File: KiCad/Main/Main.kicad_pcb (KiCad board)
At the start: 2 copper layers, 78 x 69.5 mm, 0 parts

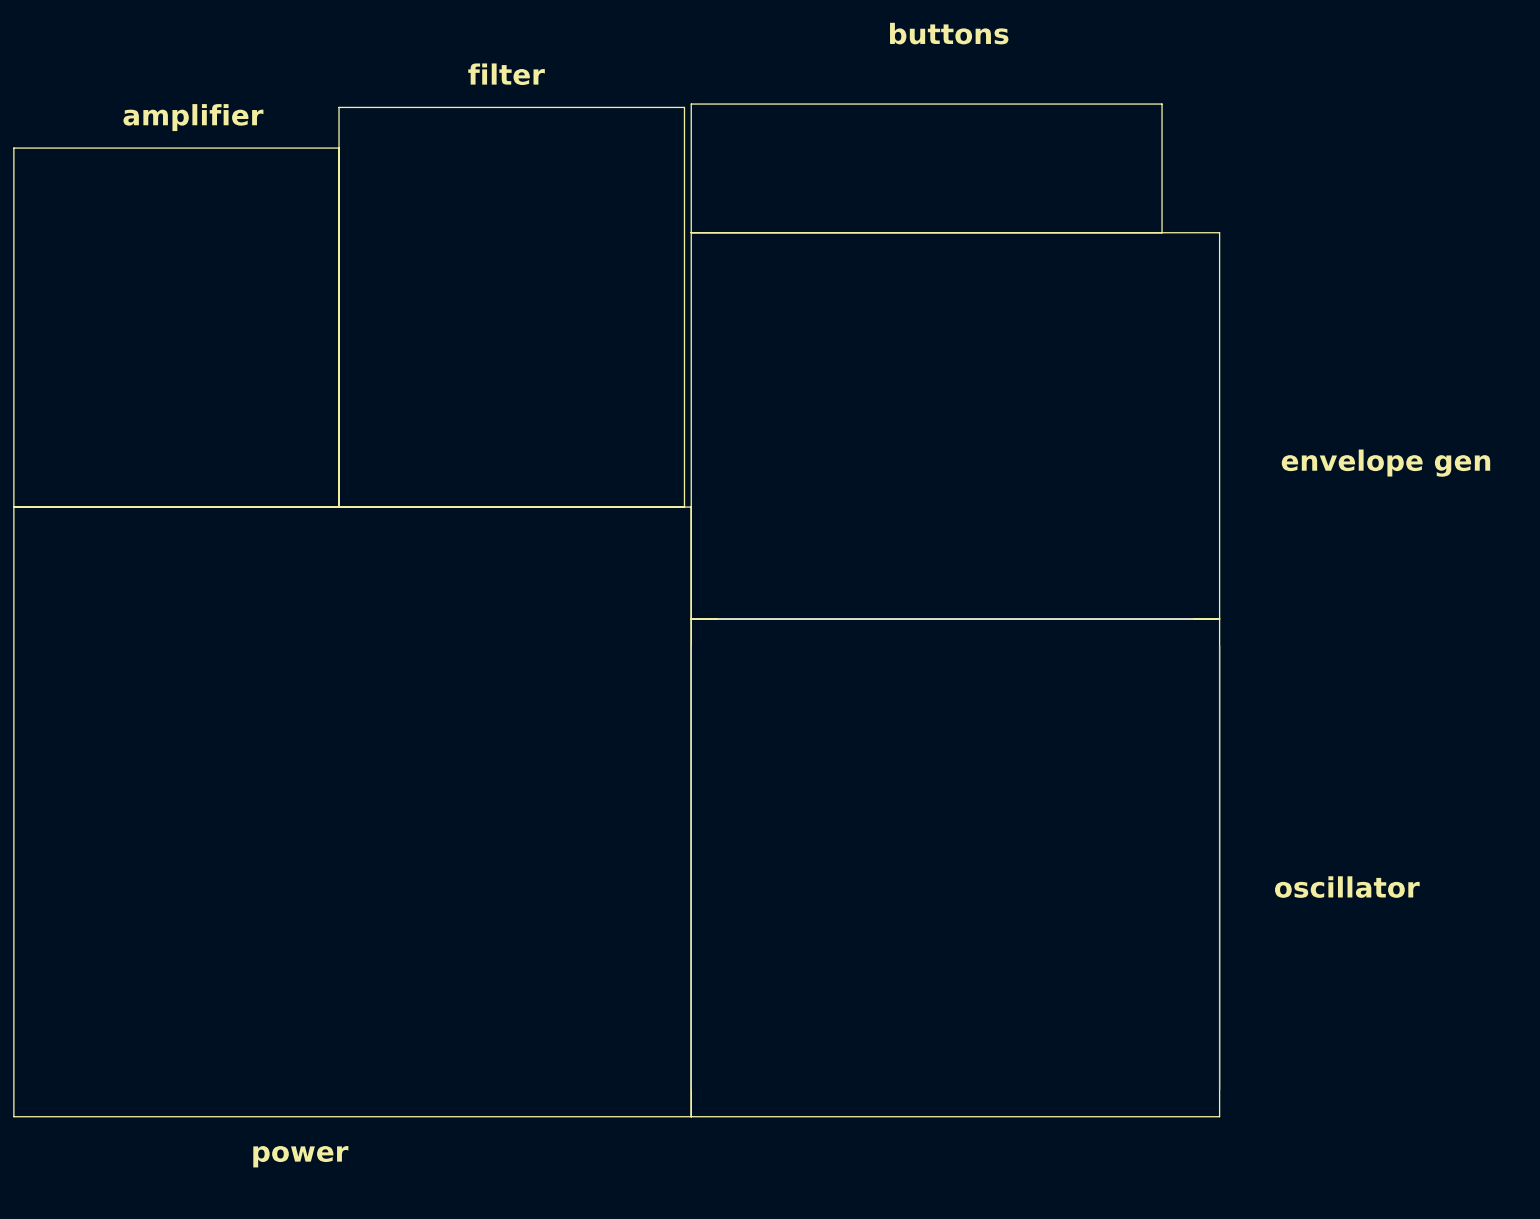
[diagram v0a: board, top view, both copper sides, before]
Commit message: merged project into one combined board (excluding the buttons)
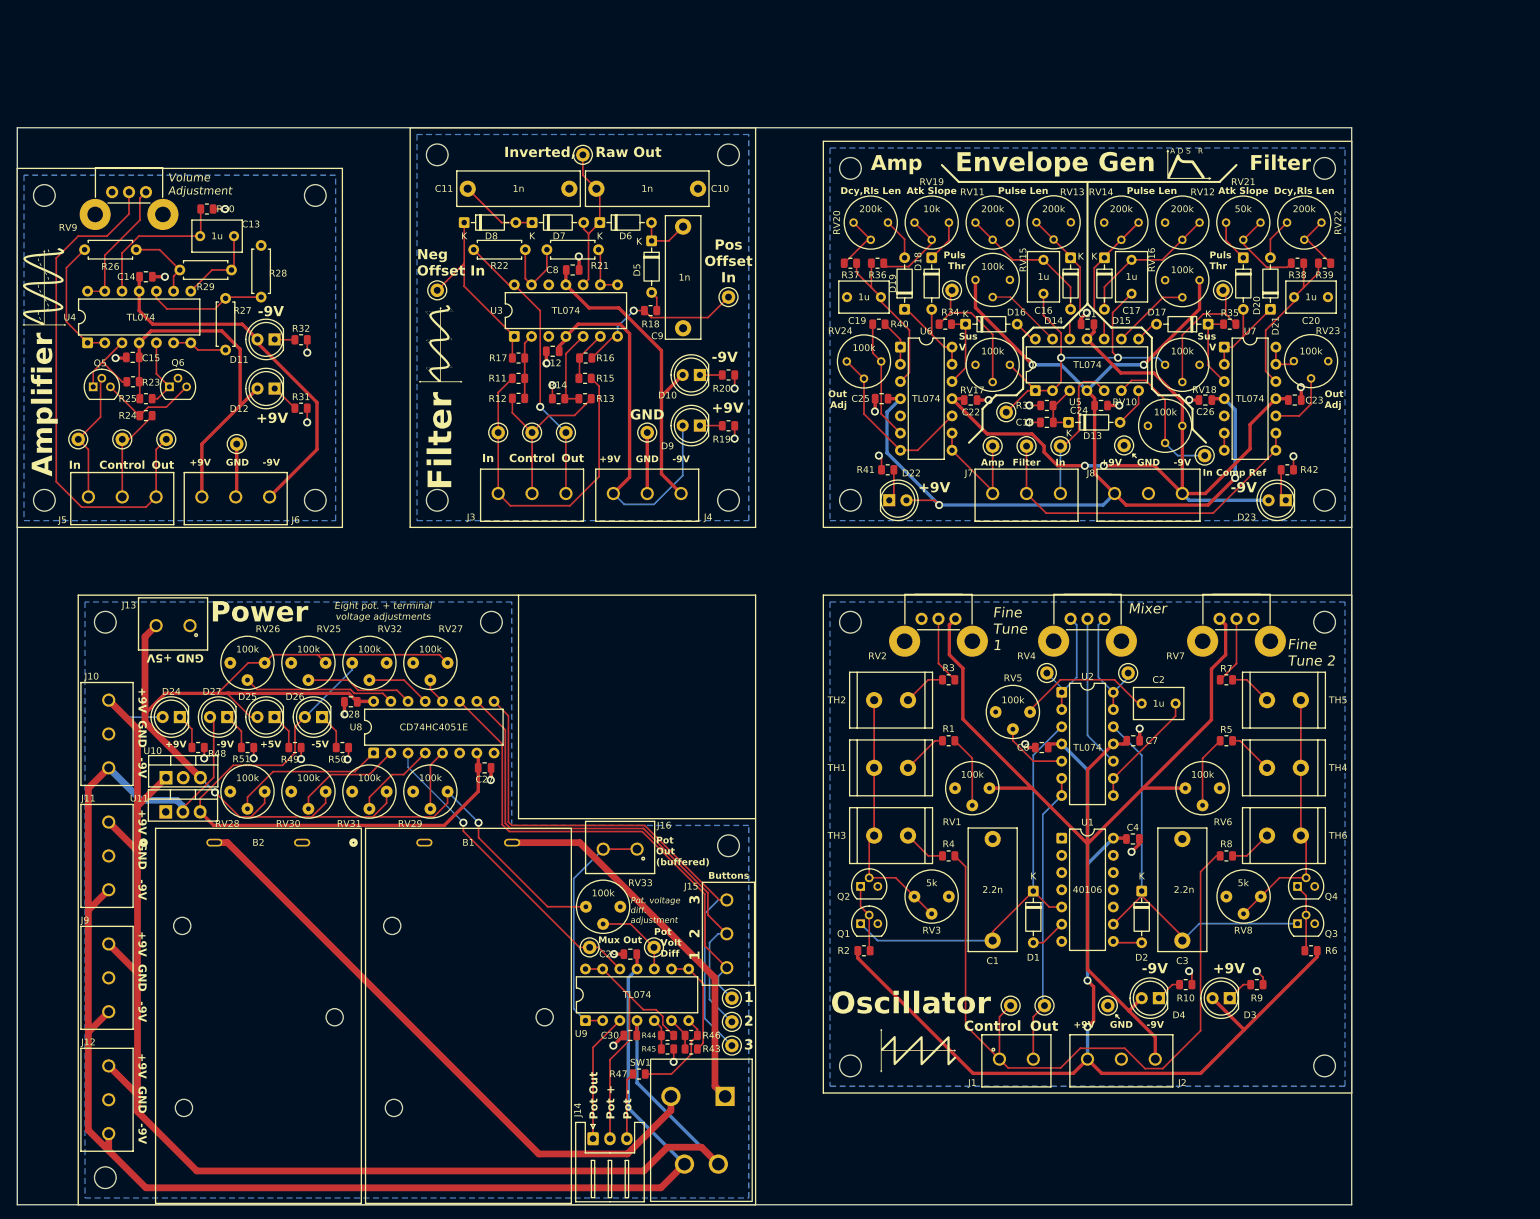
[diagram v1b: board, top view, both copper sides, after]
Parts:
- added B1: BC9VPC, Battery Holder BC9VPC:BC9VPC_MPD, F.Cu at (78.6, 124.5)
- added B2: BC9VPC, Battery Holder BC9VPC:BC9VPC_MPD, F.Cu at (47.6, 124.5)
- added C1: 2.2n, Capacitor_THT:C_Rect_L18.0mm_W7.0mm_P15.00mm_FKS3_FKP3, F.Cu at (162.5, 139.0)
- added C10: 1n, Capacitor_THT:C_Rect_L18.0mm_W5.0mm_P15.00mm_FKS3_FKP3, F.Cu at (119.0, 28.0)
- added C11: 1n, Capacitor_THT:C_Rect_L18.0mm_W5.0mm_P15.00mm_FKS3_FKP3, F.Cu at (100.0, 28.0)
- added C12: 0.1u, Capacitor_SMD:C_0805_2012Metric, F.Cu at (97.5, 52.0)
- added C13: 1u, Capacitor_THT:C_Rect_L7.2mm_W4.5mm_P5.00mm, F.Cu at (50.5, 35.0)
- added C14: 0.1u, Capacitor_SMD:C_0805_2012Metric, F.Cu at (37.5, 41.0)
- added C15: 0.1u, Capacitor_SMD:C_0805_2012Metric, F.Cu at (35.5, 52.9)
- added C16: 1u, Capacitor_THT:C_Rect_L7.2mm_W4.5mm_P5.00mm, F.Cu at (170.0, 43.5)
- added C17: 1u, Capacitor_THT:C_Rect_L7.2mm_W4.5mm_P5.00mm, F.Cu at (183.0, 43.5)
- added C18: 10n, Capacitor_SMD:C_0805_2012Metric, F.Cu at (170.5, 62.5)
- added C19: 1u, Capacitor_THT:C_Rect_L7.2mm_W4.5mm_P5.00mm, F.Cu at (141.0, 44.0)
- added C2: 1u, Capacitor_THT:C_Rect_L7.2mm_W4.5mm_P5.00mm, F.Cu at (189.5, 104.0)
- added C20: 1u, Capacitor_THT:C_Rect_L7.2mm_W4.5mm_P5.00mm, F.Cu at (212.0, 44.0)
- added C21: 0.1u, Capacitor_SMD:C_0805_2012Metric, F.Cu at (176.5, 48.0)
- added C22: 0.1u, Capacitor_SMD:C_0805_2012Metric, F.Cu at (159.2, 59.2)
- added C23: 0.1u, Capacitor_SMD:C_0805_2012Metric, F.Cu at (207.1, 59.2)
- added C24: 0.1u, Capacitor_SMD:C_0805_2012Metric, F.Cu at (178.5, 60.0)
- added C25: 0.1u, Capacitor_SMD:C_0805_2012Metric, F.Cu at (146.1, 59.0)
- added C26: 0.1u, Capacitor_SMD:C_0805_2012Metric, F.Cu at (193.9, 59.2)
- added C27: 0.1u, Capacitor_SMD:C_0805_2012Metric, F.Cu at (87.5, 113.5)
- added C28: 0.1u, Capacitor_SMD:C_0805_2012Metric, F.Cu at (67.8, 103.8)
- added C29: 0.1u, Capacitor_SMD:C_0805_2012Metric, F.Cu at (109.0, 141.0)
- added C3: 2.2n, Capacitor_THT:C_Rect_L18.0mm_W7.0mm_P15.00mm_FKS3_FKP3, F.Cu at (190.5, 139.0)
- added C30: 0.1u, Capacitor_SMD:C_0805_2012Metric, F.Cu at (109.0, 153.0)
- added C4: 0.1u, Capacitor_SMD:C_0805_2012Metric, F.Cu at (183.2, 124.0)
- added C6: 0.1u, Capacitor_SMD:C_0805_2012Metric, F.Cu at (169.8, 110.5)
- added C7: 0.1u, Capacitor_SMD:C_0805_2012Metric, F.Cu at (183.2, 109.5)
- added C8: 0.1u, Capacitor_SMD:C_0805_2012Metric, F.Cu at (100.5, 40.0)
- added C9: 1n, Capacitor_THT:C_Rect_L18.0mm_W5.0mm_P15.00mm_FKS3_FKP3, F.Cu at (116.8, 48.6)
- added D1: 1N4148, Diode_THT:D_DO-35_SOD27_P7.62mm_Horizontal, F.Cu at (168.5, 131.7)
- added D10: LED, LED_THT:LED_D5.0mm, F.Cu at (119.3, 55.5)
- added D11: LED, LED_THT:LED_D5.0mm, F.Cu at (56.5, 57.5)
- added D12: LED, LED_THT:LED_D5.0mm, F.Cu at (56.5, 50.2)
- added D13: 1N4148, Diode_THT:D_DO-35_SOD27_P7.62mm_Horizontal, F.Cu at (173.7, 62.5)
- added D14: 1N4148, Diode_THT:D_DO-35_SOD27_P7.62mm_Horizontal, F.Cu at (174.0, 38.2)
- added D15: 1N4148, Diode_THT:D_DO-35_SOD27_P7.62mm_Horizontal, F.Cu at (179.0, 38.2)
- added D16: 1N4148, Diode_THT:D_DO-35_SOD27_P7.62mm_Horizontal, F.Cu at (158.5, 48.0)
- added D17: 1N4148, Diode_THT:D_DO-35_SOD27_P7.62mm_Horizontal, F.Cu at (194.3, 48.0)
- added D18: 1N4148, Diode_THT:D_DO-35_SOD27_P7.62mm_Horizontal, F.Cu at (153.5, 38.2)
- added D19: 1N4148, Diode_THT:D_DO-35_SOD27_P7.62mm_Horizontal, F.Cu at (149.5, 45.8)
- added D2: 1N4148, Diode_THT:D_DO-35_SOD27_P7.62mm_Horizontal, F.Cu at (184.5, 131.7)
- added D20: 1N4148, Diode_THT:D_DO-35_SOD27_P7.62mm_Horizontal, F.Cu at (199.5, 38.2)
- added D21: 1N4148, Diode_THT:D_DO-35_SOD27_P7.62mm_Horizontal, F.Cu at (203.5, 45.8)
- added D22: LED, LED_THT:LED_D5.0mm, F.Cu at (147.2, 74.0)
- added D23: LED, LED_THT:LED_D5.0mm, F.Cu at (205.8, 74.0)
- added D24: LED, LED_THT:LED_D5.0mm, F.Cu at (42.5, 106.0)
- added D25: LED, LED_THT:LED_D5.0mm, F.Cu at (56.5, 106.0)
- added D26: LED, LED_THT:LED_D5.0mm, F.Cu at (63.5, 106.0)
- added D27: LED, LED_THT:LED_D5.0mm, F.Cu at (49.5, 106.0)
- added D3: LED, LED_THT:LED_D5.0mm, F.Cu at (197.5, 147.5)
- added D4: LED, LED_THT:LED_D5.0mm, F.Cu at (187.0, 147.5)
- added D5: 1N4148, Diode_THT:D_DO-35_SOD27_P7.62mm_Horizontal, F.Cu at (112.2, 35.7)
- added D6: 1N4148, Diode_THT:D_DO-35_SOD27_P7.62mm_Horizontal, F.Cu at (104.5, 33.0)
- added D7: 1N4148, Diode_THT:D_DO-35_SOD27_P7.62mm_Horizontal, F.Cu at (94.5, 33.0)
- added D8: 1N4148, Diode_THT:D_DO-35_SOD27_P7.62mm_Horizontal, F.Cu at (84.5, 33.0)
- added D9: LED, LED_THT:LED_D5.0mm, F.Cu at (119.3, 63.0)
- added G***: LOGO, LOGO, F.Cu at (22.4, 41.1)
- added G***: LOGO, LOGO, F.Cu at (197.7, 26.3)
- added G***: LOGO, LOGO, F.Cu at (153.0, 155.1)
- added G***: LOGO, LOGO, F.Cu at (80.9, 49.5)
- added H1: MountingHole_3.2mm_M3, MountingHole:MountingHole_3.2mm_M3, F.Cu at (141.5, 92.0)
- added H10: MountingHole, MountingHole:MountingHole_3.2mm_M3, F.Cu at (22.5, 74.0)
- added H11: MountingHole, MountingHole:MountingHole_3.2mm_M3, F.Cu at (62.5, 74.0)
- added H12: MountingHole, MountingHole:MountingHole_3.2mm_M3, F.Cu at (62.5, 29.0)
- added H13: MountingHole, MountingHole:MountingHole_3.2mm_M3, F.Cu at (141.5, 25.0)
- added H14: MountingHole, MountingHole:MountingHole_3.2mm_M3, F.Cu at (141.5, 74.0)
- added H15: MountingHole, MountingHole:MountingHole_3.2mm_M3, F.Cu at (211.5, 74.0)
- added H16: MountingHole, MountingHole:MountingHole_3.2mm_M3, F.Cu at (211.5, 25.0)
- added H17: MountingHole, MountingHole:MountingHole_3.2mm_M3, F.Cu at (31.5, 92.0)
- added H18: MountingHole, MountingHole:MountingHole_3.2mm_M3, F.Cu at (31.5, 174.0)
- added H19: MountingHole, MountingHole:MountingHole_3.2mm_M3, F.Cu at (123.5, 125.0)
- added H2: MountingHole_3.2mm_M3, MountingHole:MountingHole_3.2mm_M3, F.Cu at (141.5, 157.5)
- added H20: MountingHole, MountingHole:MountingHole_3.2mm_M3, F.Cu at (88.5, 92.0)
- added H3: MountingHole_3.2mm_M3, MountingHole:MountingHole_3.2mm_M3, F.Cu at (211.5, 157.5)
- added H4: MountingHole_3.2mm_M3, MountingHole:MountingHole_3.2mm_M3, F.Cu at (211.5, 92.0)
- added H5: MountingHole, MountingHole:MountingHole_3.2mm_M3, F.Cu at (80.5, 23.0)
- added H6: MountingHole, MountingHole:MountingHole_3.2mm_M3, F.Cu at (80.5, 74.0)
- added H7: MountingHole, MountingHole:MountingHole_3.2mm_M3, F.Cu at (123.5, 23.0)
- added H8: MountingHole, MountingHole:MountingHole_3.2mm_M3, F.Cu at (123.5, 74.0)
- added H9: MountingHole, MountingHole:MountingHole_3.2mm_M3, F.Cu at (22.5, 29.0)
- added J1: Screw_Terminal_01x02, Header 691137710002:691137710002, F.Cu at (166.0, 156.5)
- added J10: Screw_Terminal_01x03, Header 691137710003:691137710003, F.Cu at (32.0, 108.5)
- added J11: Screw_Terminal_01x03, Header 691137710003:691137710003, F.Cu at (32.0, 126.5)
- added J12: Screw_Terminal_01x03, Header 691137710003:691137710003, F.Cu at (32.0, 162.5)
- added J13: Screw_Terminal_01x02, Header 691137710002:691137710002, F.Cu at (41.5, 92.5)
- added J14: Conn_01x03, Connector_JST:JST_XH_S3B-XH-A_1x03_P2.50mm_Horizontal, F.Cu at (103.5, 168.2)
- added J15: Screw_Terminal_01x03, Header 691137710003:691137710003, F.Cu at (123.2, 138.0)
- added J16: Screw_Terminal_01x02, Header 691137710002:691137710002, F.Cu at (107.5, 125.5)
- added J2: Screw_Terminal_01x03, Header 691137710003:691137710003, F.Cu at (181.5, 156.5)
- added J3: Screw_Terminal_01x03, Header 691137710003:691137710003, F.Cu at (94.5, 73.0)
- added J4: Screw_Terminal_01x03, Header 691137710003:691137710003, F.Cu at (111.5, 73.0)
- added J5: Screw_Terminal_01x03, Header 691137710003:691137710003, F.Cu at (34.0, 73.5)
- added J6: Screw_Terminal_01x03, Header 691137710003:691137710003, F.Cu at (50.8, 73.5)
- added J7: Screw_Terminal_01x03, Header 691137710003:691137710003, F.Cu at (167.5, 73.0)
- added J8: Screw_Terminal_01x03, Header 691137710003:691137710003, F.Cu at (185.5, 73.0)
- added J9: Screw_Terminal_01x03, Header 691137710003:691137710003, F.Cu at (32.0, 144.5)
- added Q1: NPN, Package_TO_SOT_THT:TO-92, F.Cu at (143.0, 136.5)
- added Q2: PNP, Package_TO_SOT_THT:TO-92, F.Cu at (143.0, 131.0)
- added Q3: NPN, Package_TO_SOT_THT:TO-92, F.Cu at (207.5, 136.5)
- added Q4: PNP, Package_TO_SOT_THT:TO-92, F.Cu at (207.5, 131.0)
- added Q5: NPN, Package_TO_SOT_THT:TO-92, F.Cu at (29.7, 57.2)
- added Q6: NPN, Package_TO_SOT_THT:TO-92, F.Cu at (41.0, 57.2)
- added R1: 100k, Resistor_SMD:R_0805_2012Metric, F.Cu at (156.0, 109.5)
- added R10: 1k, Resistor_SMD:R_0805_2012Metric, F.Cu at (191.0, 145.5)
- added R11: 10k, Resistor_SMD:R_0805_2012Metric, F.Cu at (92.5, 56.0)
- added R12: 10k, Resistor_SMD:R_0805_2012Metric, F.Cu at (92.5, 59.0)
- added R13: 10k, Resistor_SMD:R_0805_2012Metric, F.Cu at (102.3, 59.0)
- added R14: 10k, Resistor_SMD:R_0805_2012Metric, F.Cu at (98.4, 59.0)
- added R15: 10k, Resistor_SMD:R_0805_2012Metric, F.Cu at (102.3, 56.0)
- added R16: 10k, Resistor_SMD:R_0805_2012Metric, F.Cu at (102.4, 53.0)
- added R17: 10k, Resistor_SMD:R_0805_2012Metric, F.Cu at (92.5, 53.0)
- added R18: 2.2k, Resistor_SMD:R_0805_2012Metric, F.Cu at (112.0, 46.0)
- added R19: 1k, Resistor_SMD:R_0805_2012Metric, F.Cu at (123.5, 63.0)
- added R2: 1M, Resistor_SMD:R_0805_2012Metric, F.Cu at (143.5, 140.5)
- added R20: 1k, Resistor_SMD:R_0805_2012Metric, F.Cu at (123.5, 55.5)
- added R21: 10k, Resistor_THT:R_Axial_DIN0207_L6.3mm_D2.5mm_P7.62mm_Horizontal, F.Cu at (104.3, 37.0)
- added R22: 1k, Resistor_THT:R_Axial_DIN0207_L6.3mm_D2.5mm_P7.62mm_Horizontal, F.Cu at (93.5, 37.0)
- added R23: 100k, Resistor_SMD:R_0805_2012Metric, F.Cu at (35.6, 56.5)
- added R24: 10k, Resistor_SMD:R_0805_2012Metric, F.Cu at (37.5, 61.5)
- added R25: 100k, Resistor_SMD:R_0805_2012Metric, F.Cu at (37.5, 59.0)
- added R26: 2.7k, Resistor_THT:R_Axial_DIN0207_L6.3mm_D2.5mm_P7.62mm_Horizontal, F.Cu at (28.4, 37.0)
- added R27: 2.7k, Resistor_THT:R_Axial_DIN0207_L6.3mm_D2.5mm_P7.62mm_Horizontal, F.Cu at (49.2, 51.8)
- added R28: 10k, Resistor_THT:R_Axial_DIN0207_L6.3mm_D2.5mm_P7.62mm_Horizontal, F.Cu at (54.5, 44.0)
- added R29: 10k, Resistor_THT:R_Axial_DIN0207_L6.3mm_D2.5mm_P7.62mm_Horizontal, F.Cu at (42.5, 40.0)
- added R3: 1M, Resistor_SMD:R_0805_2012Metric, F.Cu at (156.0, 100.5)
- added R30: 100k, Resistor_SMD:R_0805_2012Metric, F.Cu at (46.5, 31.0)
- added R31: 1k, Resistor_SMD:R_0805_2012Metric, F.Cu at (60.4, 60.4)
- added R32: 1k, Resistor_SMD:R_0805_2012Metric, F.Cu at (60.4, 50.3)
- added R33: 100k, Resistor_SMD:R_0805_2012Metric, F.Cu at (170.5, 60.0)
- added R34: 100k, Resistor_SMD:R_0805_2012Metric, F.Cu at (155.5, 48.0)
- added R35: 100k, Resistor_SMD:R_0805_2012Metric, F.Cu at (197.5, 48.0)
- added R36: 1k, Resistor_SMD:R_0805_2012Metric, F.Cu at (145.5, 39.0)
- added R37: 51k, Resistor_SMD:R_0805_2012Metric, F.Cu at (141.5, 39.0)
- added R38: 22k, Resistor_SMD:R_0805_2012Metric, F.Cu at (207.5, 39.0)
- added R39: 51k, Resistor_SMD:R_0805_2012Metric, F.Cu at (211.5, 39.0)
- added R4: 100k, Resistor_SMD:R_0805_2012Metric, F.Cu at (156.0, 126.5)
- added R40: 51k, Resistor_SMD:R_0805_2012Metric, F.Cu at (145.7, 48.0)
- added R41: 1k, Resistor_SMD:R_0805_2012Metric, F.Cu at (147.0, 69.5)
- added R42: 1k, Resistor_SMD:R_0805_2012Metric, F.Cu at (206.0, 69.5)
- added R43: 10k, Resistor_SMD:R_0805_2012Metric, F.Cu at (118.0, 155.0)
- added R44: 10k, Resistor_SMD:R_0805_2012Metric, F.Cu at (114.5, 153.0)
- added R45: 10k, Resistor_SMD:R_0805_2012Metric, F.Cu at (114.5, 155.0)
- added R46: 10k, Resistor_SMD:R_0805_2012Metric, F.Cu at (118.0, 153.0)
- added R47: 1k, Resistor_SMD:R_0805_2012Metric, F.Cu at (110.3, 158.7)
- added R48: 1k, Resistor_SMD:R_0805_2012Metric, F.Cu at (45.2, 110.5)
- added R49: 820, Resistor_SMD:R_0805_2012Metric, F.Cu at (59.5, 110.5)
- added R5: 100k, Resistor_SMD:R_0805_2012Metric, F.Cu at (197.0, 109.5)
- added R50: 820, Resistor_SMD:R_0805_2012Metric, F.Cu at (66.5, 110.5)
- added R51: 1k, Resistor_SMD:R_0805_2012Metric, F.Cu at (52.5, 110.5)
- added R6: 1M, Resistor_SMD:R_0805_2012Metric, F.Cu at (209.5, 140.5)
- added R7: 1M, Resistor_SMD:R_0805_2012Metric, F.Cu at (197.0, 100.5)
- added R8: 100k, Resistor_SMD:R_0805_2012Metric, F.Cu at (197.0, 126.5)
- added R9: 1k, Resistor_SMD:R_0805_2012Metric, F.Cu at (201.5, 145.5)
- added RV1: 100k, Potentiometer_THT:Potentiometer_Bourns_3339P_Vertical_HandSoldering, F.Cu at (162.0, 116.5)
- added RV10: 100k, Potentiometer_THT:Potentiometer_Bourns_3339P_Vertical, F.Cu at (190.5, 63.0)
- added RV11: 200k, Potentiometer_THT:Potentiometer_Bourns_3339P_Vertical, F.Cu at (165.0, 33.0)
- added RV12: 200k, Potentiometer_THT:Potentiometer_Bourns_3339P_Vertical, F.Cu at (193.0, 33.0)
- added RV13: 200k, Potentiometer_THT:Potentiometer_Bourns_3339P_Vertical, F.Cu at (174.0, 33.0)
- added RV14: 200k, Potentiometer_THT:Potentiometer_Bourns_3339P_Vertical, F.Cu at (184.0, 33.0)
- added RV15: 100k, Potentiometer_THT:Potentiometer_Bourns_3339P_Vertical, F.Cu at (165.0, 41.5)
- added RV16: 100k, Potentiometer_THT:Potentiometer_Bourns_3339P_Vertical, F.Cu at (193.0, 41.5)
- added RV17: 100k, Potentiometer_THT:Potentiometer_Bourns_3339P_Vertical, F.Cu at (165.0, 54.0)
- added RV18: 100k, Potentiometer_THT:Potentiometer_Bourns_3339P_Vertical, F.Cu at (193.0, 54.0)
- added RV19: 10k, Potentiometer_THT:Potentiometer_Bourns_3339P_Vertical, F.Cu at (156.0, 33.0)
- added RV2: 100k, Potentiometer_THT:Potentiometer_Bourns_PTV09A-2_Single_Horizontal, F.Cu at (157.0, 91.5)
- added RV20: 200k, Potentiometer_THT:Potentiometer_Bourns_3339P_Vertical, F.Cu at (147.0, 33.0)
- added RV21: 50k, Potentiometer_THT:Potentiometer_Bourns_3339P_Vertical, F.Cu at (202.0, 33.0)
- added RV22: 200k, Potentiometer_THT:Potentiometer_Bourns_3339P_Vertical, F.Cu at (211.0, 33.0)
- added RV23: 100k, Potentiometer_THT:Potentiometer_Bourns_3339P_Vertical, F.Cu at (212.0, 53.5)
- added RV24: 100k, Potentiometer_THT:Potentiometer_Bourns_3339P_Vertical, F.Cu at (146.0, 53.5)
- added RV25: 100k, Potentiometer_THT:Potentiometer_Bourns_3339P_Vertical_HandSoldering, F.Cu at (64.0, 98.0)
- added RV26: 100k, Potentiometer_THT:Potentiometer_Bourns_3339P_Vertical_HandSoldering, F.Cu at (55.0, 98.0)
- added RV27: 100k, Potentiometer_THT:Potentiometer_Bourns_3339P_Vertical_HandSoldering, F.Cu at (82.0, 98.0)
- added RV28: 100k, Potentiometer_THT:Potentiometer_Bourns_3339P_Vertical_HandSoldering, F.Cu at (55.0, 117.0)
- added RV29: 100k, Potentiometer_THT:Potentiometer_Bourns_3339P_Vertical_HandSoldering, F.Cu at (82.0, 117.0)
- added RV3: 5k, Potentiometer_THT:Potentiometer_Bourns_3339P_Vertical_HandSoldering, F.Cu at (156.0, 132.5)
- added RV30: 100k, Potentiometer_THT:Potentiometer_Bourns_3339P_Vertical_HandSoldering, F.Cu at (64.0, 117.0)
- added RV31: 100k, Potentiometer_THT:Potentiometer_Bourns_3339P_Vertical_HandSoldering, F.Cu at (73.0, 117.0)
- added RV32: 100k, Potentiometer_THT:Potentiometer_Bourns_3339P_Vertical_HandSoldering, F.Cu at (73.0, 98.0)
- added RV33: 100k, Potentiometer_THT:Potentiometer_Bourns_3339P_Vertical_HandSoldering, F.Cu at (107.5, 134.0)
- added RV4: 100k, Potentiometer_THT:Potentiometer_Bourns_PTV09A-2_Single_Horizontal, F.Cu at (179.0, 91.5)
- added RV5: 100k, Potentiometer_THT:Potentiometer_Bourns_3339P_Vertical_HandSoldering, F.Cu at (168.0, 105.2)
- added RV6: 100k, Potentiometer_THT:Potentiometer_Bourns_3339P_Vertical_HandSoldering, F.Cu at (196.0, 116.5)
- added RV7: 100k, Potentiometer_THT:Potentiometer_Bourns_PTV09A-2_Single_Horizontal, F.Cu at (201.0, 91.5)
- added RV8: 5k, Potentiometer_THT:Potentiometer_Bourns_3339P_Vertical_HandSoldering, F.Cu at (202.1, 132.5)
- added RV9: 100k, Potentiometer_THT:Potentiometer_Bourns_PTV09A-2_Single_Horizontal, F.Cu at (37.5, 28.5)
- added SW1: SW_DPST, Library:DPST Switch RA83231100, F.Cu at (119.5, 167.0)
- added TH1: 10k, Resistor_THT:R_Radial_Power_L12.0mm_W8.0mm_P5.00mm, F.Cu at (150.0, 113.5)
- added TH2: 10k, Resistor_THT:R_Radial_Power_L12.0mm_W8.0mm_P5.00mm, F.Cu at (150.0, 103.5)
- added TH3: 10k, Resistor_THT:R_Radial_Power_L12.0mm_W8.0mm_P5.00mm, F.Cu at (150.0, 123.5)
- added TH4: 10k, Resistor_THT:R_Radial_Power_L12.0mm_W8.0mm_P5.00mm, F.Cu at (203.0, 113.5)
- added TH5: 10k, Resistor_THT:R_Radial_Power_L12.0mm_W8.0mm_P5.00mm, F.Cu at (203.0, 103.5)
- added TH6: 10k, Resistor_THT:R_Radial_Power_L12.0mm_W8.0mm_P5.00mm, F.Cu at (203.0, 123.5)
- added TP1: TestPoint_Small, TestPoint:TestPoint_Keystone_5000-5004_Miniature, F.Cu at (170.5, 99.5)
- added TP10: TestPoint_Small, TestPoint:TestPoint_Keystone_5000-5004_Miniature, F.Cu at (123.5, 44.0)
- added TP11: TestPoint_Small, TestPoint:TestPoint_Keystone_5000-5004_Miniature, F.Cu at (80.5, 43.0)
- added TP12: TestPoint_Small, TestPoint:TestPoint_Keystone_5000-5004_Miniature, F.Cu at (102.0, 23.0)
- added TP13: TestPoint_Small, TestPoint:TestPoint_Keystone_5000-5004_Miniature, F.Cu at (27.5, 65.0)
- added TP14: TestPoint_Small, TestPoint:TestPoint_Keystone_5000-5004_Miniature, F.Cu at (34.0, 65.0)
- added TP15: TestPoint_Small, TestPoint:TestPoint_Keystone_5000-5004_Miniature, F.Cu at (40.5, 65.0)
- added TP16: TestPoint_Small, TestPoint:TestPoint_Keystone_5000-5004_Miniature, F.Cu at (50.9, 65.7)
- added TP17: TestPoint_Small, TestPoint:TestPoint_Keystone_5000-5004_Miniature, F.Cu at (193.8, 67.4)
- added TP18: TestPoint_Small, TestPoint:TestPoint_Keystone_5000-5004_Miniature, F.Cu at (164.5, 61.0)
- added TP19: TestPoint_Small, TestPoint:TestPoint_Keystone_5000-5004_Miniature, F.Cu at (156.5, 43.0)
- added TP2: TestPoint_Small, TestPoint:TestPoint_Keystone_5000-5004_Miniature, F.Cu at (182.5, 99.5)
- added TP20: TestPoint_Small, TestPoint:TestPoint_Keystone_5000-5004_Miniature, F.Cu at (196.5, 43.0)
- added TP21: TestPoint_Small, TestPoint:TestPoint_Keystone_5000-5004_Miniature, F.Cu at (162.5, 66.0)
- added TP22: TestPoint_Small, TestPoint:TestPoint_Keystone_5000-5004_Miniature, F.Cu at (167.5, 66.0)
- added TP23: TestPoint_Small, TestPoint:TestPoint_Keystone_5000-5004_Miniature, F.Cu at (172.5, 66.0)
- added TP24: TestPoint_Small, TestPoint:TestPoint_Keystone_5000-5004_Miniature, F.Cu at (181.9, 65.9)
- added TP25: TestPoint_Small, TestPoint:TestPoint_Keystone_5000-5004_Miniature, F.Cu at (124.0, 147.5)
- added TP26: TestPoint_Small, TestPoint:TestPoint_Keystone_5000-5004_Miniature, F.Cu at (124.0, 151.0)
- added TP27: TestPoint_Small, TestPoint:TestPoint_Keystone_5000-5004_Miniature, F.Cu at (124.0, 154.5)
- added TP28: TestPoint_Small, TestPoint:TestPoint_Keystone_5000-5004_Miniature, F.Cu at (103.0, 140.0)
- added TP29: TestPoint_Small, TestPoint:TestPoint_Keystone_5000-5004_Miniature, F.Cu at (112.5, 140.0)
- added TP3: TestPoint_Small, TestPoint:TestPoint_Keystone_5000-5004_Miniature, F.Cu at (165.2, 148.6)
- added TP4: TestPoint_Small, TestPoint:TestPoint_Keystone_5000-5004_Miniature, F.Cu at (170.2, 148.6)
- added TP5: TestPoint_Small, TestPoint:TestPoint_Keystone_5000-5004_Miniature, F.Cu at (179.5, 148.6)
- added TP6: TestPoint_Small, TestPoint:TestPoint_Keystone_5000-5004_Miniature, F.Cu at (89.5, 64.0)
- added TP7: TestPoint_Small, TestPoint:TestPoint_Keystone_5000-5004_Miniature, F.Cu at (94.5, 64.0)
- added TP8: TestPoint_Small, TestPoint:TestPoint_Keystone_5000-5004_Miniature, F.Cu at (99.5, 64.0)
- added TP9: TestPoint_Small, TestPoint:TestPoint_Keystone_5000-5004_Miniature, F.Cu at (111.5, 64.0)
- added U1: 40106, Package_DIP:DIP-14_W7.62mm, F.Cu at (172.7, 123.9)
- added U10: L7805, Package_TO_SOT_THT:TO-220-3_Vertical, F.Cu at (40.5, 115.0)
- added U11: L7905, Package_TO_SOT_THT:TO-220-3_Vertical, F.Cu at (40.4, 120.0)
- added U2: TL074, Package_DIP:DIP-14_W7.62mm, F.Cu at (172.7, 102.3)
- added U3: TL074, Package_DIP:DIP-14_W7.62mm, F.Cu at (91.9, 49.8)
- added U4: TL074, Package_DIP:DIP-14_W7.62mm, F.Cu at (28.9, 50.8)
- added U5: TL074, Package_DIP:DIP-14_W7.62mm, F.Cu at (168.8, 57.8)
- added U6: TL074, Package_DIP:DIP-14_W7.62mm, F.Cu at (148.9, 51.4)
- added U7: TL074, Package_DIP:DIP-14_W7.62mm, F.Cu at (196.7, 51.4)
- added U8: CD74HC4051E, Package_DIP:DIP-16_W7.62mm, F.Cu at (71.1, 111.3)
- added U9: TL074, Package_DIP:DIP-14_W7.62mm, F.Cu at (102.4, 150.8)
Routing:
- net +9V: track 0.00 -> 633.7 mm, vias 0 -> 6
- net -9V: track 0.00 -> 591.2 mm, vias 0 -> 2
- net +5V: track 0.00 -> 190.9 mm, vias 0 -> 2
- net /Out: track 0.00 -> 118.0 mm, vias 0 -> 1
- net /Oscillator/Control: track 0.00 -> 103.6 mm
- net Net-(B2-Pad1): track 0.00 -> 91.2 mm
- net -5V: track 0.00 -> 85.3 mm
- net /Button 3: track 0.00 -> 80.9 mm
- net GND: track 0.00 -> 80.6 mm, vias 0 -> 34
- net /Button 2: track 0.00 -> 77.3 mm
- net /Button 1: track 0.00 -> 73.0 mm
- net /In: track 0.00 -> 69.9 mm
- net /Oscillator/Sch Inv In 1: track 0.00 -> 61.5 mm
- net /Oscillator/Sch Inv In 2: track 0.00 -> 59.8 mm
- net Net-(B1-Pad2): track 0.00 -> 56.3 mm
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- added copper zone on B.Cu, net GND
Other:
- board size 78 x 69.5 mm -> 197 x 159 mm
- board text added: "+5V"
- board text added: "+9V"
- board text added: "-5V"
- board text added: "-9V"
- board text added: "1"
- board text added: "100k"
- board text added: "10k"
- board text added: "2"
- board text added: "200k"
- board text added: "3"
- board text added: "50k"
- board text added: "A"
- board text added: "Amp"
- board text added: "Amplifier"
- board text added: "Atk Slope"
- board text added: "Buttons"
- board text added: "Control"
- board text added: "D"
- board text added: "Dcy,Rls Len"
- board text added: "Eight pot. + terminal voltage adjustments"
- board text added: "Envelope Gen"
- board text added: "Filter"
- board text added: "Fine Tune 1"
- board text added: "Fine Tune 2"
- board text added: "GND"
- board text added: "In"
- board text added: "In Comp Ref"
- board text added: "Inverted, Raw Out"
- board text added: "Mixer"
- board text added: "Mux Out"
- board text added: "Neg Offset In"
- board text added: "Oscillator"
- board text added: "Out"
- board text added: "Out Adj"
- board text added: "Pos Offset In"
- board text added: "Pot +"
- board text added: "Pot -"
- board text added: "Pot Out"
- board text added: "Pot Out (buffered)"
- board text added: "Pot Volt Diff"
- board text added: "Pot. voltage diff. adjustment"
- board text added: "Power"
- board text added: "Puls Thr"
- board text added: "Pulse Len"
- board text added: "R"
- board text added: "S"
- board text added: "Sus V"
- board text added: "Volume Adjustment"
- board text removed: "amplifier"
- board text removed: "buttons"
- board text removed: "envelope gen"
- board text removed: "filter"
- board text removed: "oscillator"
- board text removed: "power"
